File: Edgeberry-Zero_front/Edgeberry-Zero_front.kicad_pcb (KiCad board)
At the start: 2 copper layers, 59.8 x 20.6 mm, 1 part, among them J1 PinSocket_1x04_P2.54mm_Vertic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

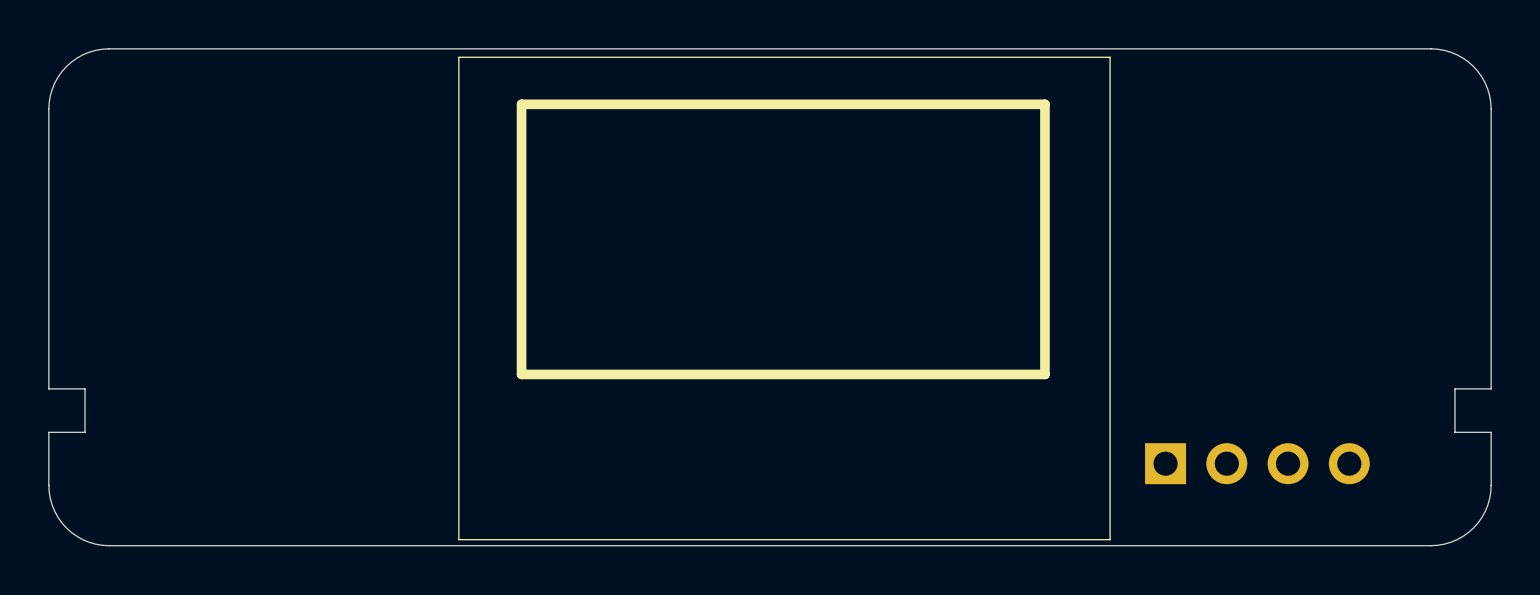
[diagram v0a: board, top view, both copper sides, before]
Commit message: Improvements: C2, J4 (ext)
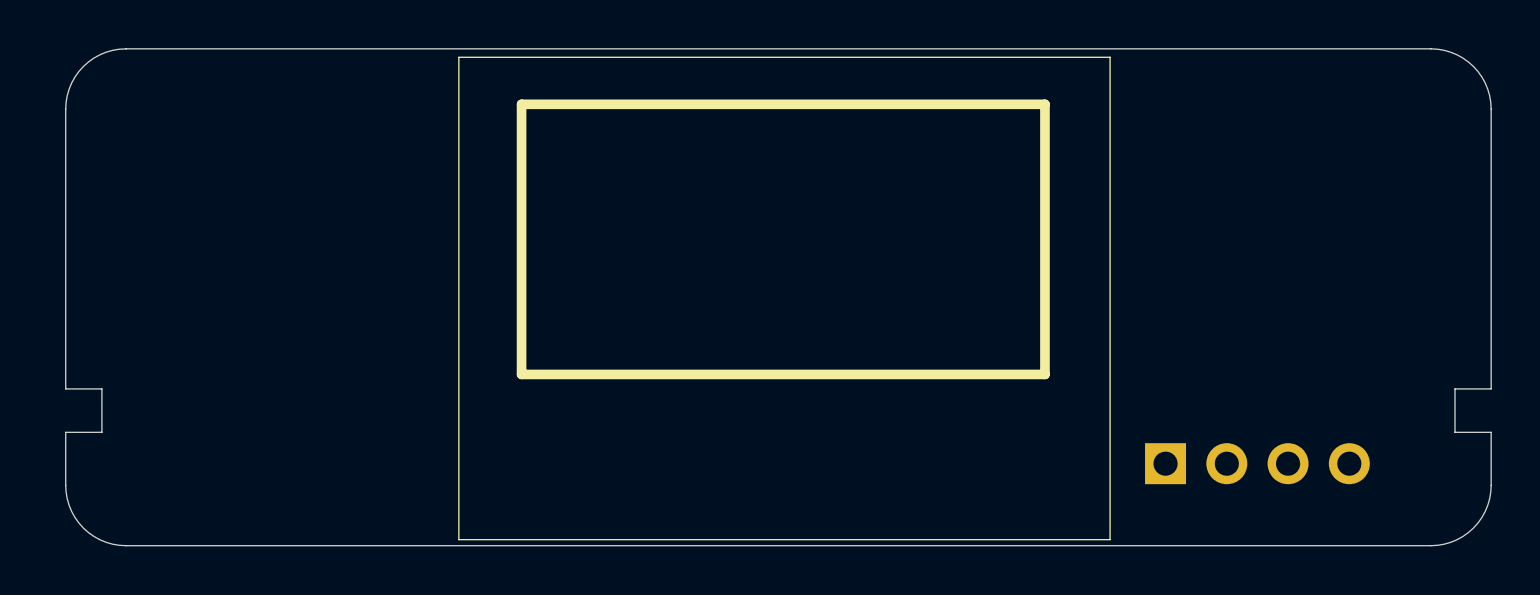
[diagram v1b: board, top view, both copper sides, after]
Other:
- board size 59.8 x 20.6 mm -> 59.1 x 20.6 mm
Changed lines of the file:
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@@
 		)
 		(property "Value" "PinSocket_1x04_P2.54mm_Vertical"
-			(at 7.8 -4.6 180)
+			(at 7.8 -4.6 0)
 			(layer "B.Fab")
 			(hide yes)
@@
 			)
 		)
+		(model "/home/tom/Projects/KiCad_library/3D models/Elecrow_display.step"
+			(offset
+				(xyz -6.9 15.8 -1.6)
+			)
+			(scale
+				(xyz 1 1 1)
+			)
+			(rotate
+				(xyz 0 180 -90)
+			)
+		)
 	)
 	(gr_poly
@@
 	(gr_line
 		(start 188.3 109.7)
-		(end 128.5 109.7)
+		(end 129.2 109.7)
 		(locked yes)
 		(stroke
@@
 	(gr_line
 		(start 186.8 115.3)
-		(end 130 115.3)
+		(end 130.7 115.3)
 		(locked yes)
 		(stroke
@@
 	(gr_line
 		(start 186.8 113.5)
-		(end 130 113.5)
+		(end 130.7 113.5)
 		(locked yes)
 		(stroke
@@
 	)
 	(gr_arc
-		(start 128.5 101.9)
-		(mid 129.232233 100.132233)
-		(end 131 99.4)
+		(start 129.2 101.9)
+		(mid 129.932233 100.132233)
+		(end 131.7 99.4)
 		(locked yes)
 		(stroke
@@
 	(gr_line
 		(start 185.8 99.4)
-		(end 131 99.4)
-		(locked yes)
-		(stroke
-			(width 0.05)
-			(type default)
-		)
-		(layer "Edge.Cuts")
-	)
-	(gr_line
-		(start 130 113.5)
-		(end 128.5 113.5)
-		(locked yes)
-		(stroke
-			(width 0.05)
-			(type default)
-		)
-		(layer "Edge.Cuts")
-	)
-	(gr_line
-		(start 130 113.5)
-		(end 130 115.3)
-		(locked yes)
-		(stroke
-			(width 0.05)
-			(type default)
-		)
-		(layer "Edge.Cuts")
-	)
-	(gr_line
-		(start 131 120)
+		(end 131.7 99.4)
+		(locked yes)
+		(stroke
+			(width 0.05)
+			(type default)
+		)
+		(layer "Edge.Cuts")
+	)
+	(gr_line
+		(start 130.7 113.5)
+		(end 129.2 113.5)
+		(locked yes)
+		(stroke
+			(width 0.05)
+			(type default)
+		)
+		(layer "Edge.Cuts")
+	)
+	(gr_line
+		(start 130.7 113.5)
+		(end 130.7 115.3)
+		(locked yes)
+		(stroke
+			(width 0.05)
+			(type default)
+		)
+		(layer "Edge.Cuts")
+	)
+	(gr_line
+		(start 131.7 120)
 		(end 185.8 120)
 		(locked yes)
@@
 	)
 	(gr_arc
-		(start 131 120)
-		(mid 129.232233 119.267767)
-		(end 128.5 117.5)
+		(start 131.7 120)
+		(mid 129.932233 119.267767)
+		(end 129.2 117.5)
 		(locked yes)
 		(stroke
@@
 	)
 	(gr_line
-		(start 130 115.3)
-		(end 128.5 115.3)
+		(start 130.7 115.3)
+		(end 129.2 115.3)
 		(locked yes)
 		(stroke
@@
 	)
 	(gr_line
-		(start 128.5 113.5)
-		(end 128.5 101.9)
+		(start 129.2 113.5)
+		(end 129.2 101.9)
 		(locked yes)
 		(stroke
@@
 	)
 	(gr_line
-		(start 128.5 117.5)
-		(end 128.5 115.3)
-		(locked yes)
-		(stroke
+		(start 129.2 117.5)
+		(end 129.2 115.3)
+		(locked yes)
+		(stroke

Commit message: cleanup
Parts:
- removed J1: PinSocket_1x04_P2.54mm_Vertical, Connector_PinSocket_2.54mm:PinSocket_1x04_P2.54mm_Vertical
- added REF**: PinHeader_1x04_P2.00mm_Vertical, Connector_PinHeader_2.00mm:PinHeader_1x04_P2.00mm_Vertical, B.Cu at (182.0, 116.3)
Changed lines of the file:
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@@
 	)
 	(net 0 "")
-	(footprint "Connector_PinSocket_2.54mm:PinSocket_1x04_P2.54mm_Vertical"
-		(locked yes)
+	(footprint "Connector_PinHeader_2.00mm:PinHeader_1x04_P2.00mm_Vertical"
 		(layer "B.Cu")
-		(at 174.8 116.6 -90)
-		(descr "Through hole straight socket strip, 1x04, 2.54mm pitch, single row (from Kicad 4.0.7), script generated")
-		(tags "Through hole socket strip THT 1x04 2.54mm single row")
-		(property "Reference" "J1"
-			(at 0 2.77 90)
+		(at 182 116.3 90)
+		(descr "Through hole straight pin header, 1x04, 2.00mm pitch, single row")
+		(tags "Through hole pin header THT 1x04 2.00mm single row")
+		(property "Reference" "REF**"
+			(at 0 2.06 90)
 			(layer "B.SilkS")
 			(effects
@@
 			)
 		)
-		(property "Value" "PinSocket_1x04_P2.54mm_Vertical"
-			(at 7.8 -4.6 0)
+		(property "Value" "PinHeader_1x04_P2.00mm_Vertical"
+			(at 0 -8.06 90)
 			(layer "B.Fab")
-			(hide yes)
 			(effects
 				(font
@@
 			)
 		)
-		(property "Footprint" "Connector_PinSocket_2.54mm:PinSocket_1x04_P2.54mm_Vertical"
-			(at 0 0 90)
+		(property "Footprint" "Connector_PinHeader_2.00mm:PinHeader_1x04_P2.00mm_Vertical"
+			(at 0 0 -90)
 			(unlocked yes)
 			(layer "B.Fab")
@@
 		)
 		(property "Datasheet" ""
-			(at 0 0 90)
+			(at 0 0 -90)
 			(unlocked yes)
 			(layer "B.Fab")
@@
 		)
 		(property "Description" ""
-			(at 0 0 90)
+			(at 0 0 -90)
 			(unlocked yes)
 			(layer "B.Fab")
@@
 		(attr through_hole)
 		(fp_line
-			(start 1.33 1.33)
-			(end 0 1.33)
+			(start 1.06 -7.06)
+			(end -1.06 -7.06)
 			(stroke
 				(width 0.12)
@@
 		)
 		(fp_line
-			(start 1.33 0)
-			(end 1.33 1.33)
+			(start 1.06 -7.06)
+			(end 1.06 -1)
 			(stroke
 				(width 0.12)
@@
 		)
 		(fp_line
-			(start 1.33 -1.27)
-			(end -1.33 -1.27)
+			(start -1.06 -7.06)
+			(end -1.06 -1)
 			(stroke
 				(width 0.12)
@@
 		)
 		(fp_line
-			(start -1.33 -8.95)
-			(end -1.33 -1.27)
+			(start 1.06 -1)
+			(end -1.06 -1)
 			(stroke
 				(width 0.12)
@@
 		)
 		(fp_line
-			(start 1.33 -8.95)
-			(end 1.33 -1.27)
+			(start 0 1.06)
+			(end -1.06 1.06)
 			(stroke
 				(width 0.12)
@@
 		)
 		(fp_line
-			(start 1.33 -8.95)
-			(end -1.33 -8.95)
+			(start -1.06 1.06)
+			(end -1.06 0)
 			(stroke
 				(width 0.12)
@@
 		)
 		(fp_line
-			(start -1.8 1.8)
-			(end -1.8 -9.4)
+			(start 1.5 -7.5)
+			(end -1.5 -7.5)
 			(stroke
 				(width 0.05)
@@
 		)
 		(fp_line
-			(start 1.75 1.8)
-			(end -1.8 1.8)
+			(start -1.5 -7.5)
+			(end -1.5 1.5)
 			(stroke
 				(width 0.05)
@@
 		)
 		(fp_line
-			(start -1.8 -9.4)
-			(end 1.75 -9.4)
+			(start 1.5 1.5)
+			(end 1.5 -7.5)
 			(stroke
 				(width 0.05)
@@
 		)
 		(fp_line
-			(start 1.75 -9.4)
-			(end 1.75 1.8)
+			(start -1.5 1.5)
+			(end 1.5 1.5)
 			(stroke
 				(width 0.05)
@@
 		)
 		(fp_line
-			(start -1.27 1.27)
-			(end -1.27 -8.89)
+			(start 1 -7)
+			(end 1 1)
 			(stroke
 				(width 0.1)
@@
 		)
 		(fp_line
-			(start 0.635 1.27)
-			(end -1.27 1.27)
+			(start -1 -7)
+			(end 1 -7)
 			(stroke
 				(width 0.1)
@@
 		)
 		(fp_line
-			(start 1.27 0.635)
-			(end 0.635 1.27)
+			(start -1 0.5)
+			(end -1 -7)
 			(stroke
 				(width 0.1)
@@
 		)
 		(fp_line
-			(start -1.27 -8.89)
-			(end 1.27 -8.89)
+			(start 1 1)
+			(end -0.5 1)
 			(stroke
 				(width 0.1)
@@
 		)
 		(fp_line
-			(start 1.27 -8.89)
-			(end 1.27 0.635)
+			(start -0.5 1)
+			(end -1 0.5)
 			(stroke
 				(width 0.1)
@@
 		)
 		(fp_text user "${REFERENCE}"
-			(at 0 -3.81 0)
+			(at 0 -3 360)
 			(layer "B.Fab")
 			(effects
@@
 		)
 		(pad "1" thru_hole rect
-			(at 0 0 270)
-			(size 1.7 1.7)
-			(drill 1)
+			(at 0 0 90)
+			(size 1.35 1.35)
+			(drill 0.8)
 			(layers "*.Cu" "*.Mask" "In1.Cu" "In2.Cu" "In3.Cu" "In4.Cu" "In5.Cu" "In6.Cu"
 				"In7.Cu" "In8.Cu" "In9.Cu" "In10.Cu" "In11.Cu" "In12.Cu" "In13.Cu" "In14.Cu"
@@
 		)
 		(pad "2" thru_hole oval
-			(at 0 -2.54 270)
-			(size 1.7 1.7)
-			(drill 1)
+			(at 0 -2 90)
+			(size 1.35 1.35)
+			(drill 0.8)
 			(layers "*.Cu" "*.Mask" "In1.Cu" "In2.Cu" "In3.Cu" "In4.Cu" "In5.Cu" "In6.Cu"
 				"In7.Cu" "In8.Cu" "In9.Cu" "In10.Cu" "In11.Cu" "In12.Cu" "In13.Cu" "In14.Cu"
@@
 		)
 		(pad "3" thru_hole oval
-			(at 0 -5.08 270)
-			(size 1.7 1.7)
-			(drill 1)
+			(at 0 -4 90)
+			(size 1.35 1.35)
+			(drill 0.8)
 			(layers "*.Cu" "*.Mask" "In1.Cu" "In2.Cu" "In3.Cu" "In4.Cu" "In5.Cu" "In6.Cu"
 				"In7.Cu" "In8.Cu" "In9.Cu" "In10.Cu" "In11.Cu" "In12.Cu" "In13.Cu" "In14.Cu"
@@
 		)
 		(pad "4" thru_hole oval
-			(at 0 -7.62 270)
-			(size 1.7 1.7)
-			(drill 1)
+			(at 0 -6 90)
+			(size 1.35 1.35)
+			(drill 0.8)
 			(layers "*.Cu" "*.Mask" "In1.Cu" "In2.Cu" "In3.Cu" "In4.Cu" "In5.Cu" "In6.Cu"
 				"In7.Cu" "In8.Cu" "In9.Cu" "In10.Cu" "In11.Cu" "In12.Cu" "In13.Cu" "In14.Cu"
@@
 			(remove_unused_layers no)
 		)
-		(model "${KICAD8_3DMODEL_DIR}/Connector_PinSocket_2.54mm.3dshapes/PinSocket_1x04_P2.54mm_Vertical.wrl"
-			(hide yes)
+		(model "${KICAD8_3DMODEL_DIR}/Connector_PinHeader_2.00mm.3dshapes/PinHeader_1x04_P2.00mm_Vertical.wrl"
 			(offset
 				(xyz 0 0 0)
@@
 			(rotate
 				(xyz 0 0 0)
-			)
-		)
-		(model "/home/tom/Projects/KiCad_library/3D models/Elecrow_display.step"
-			(offset
-				(xyz -6.9 15.8 -1.6)
-			)
-			(scale
-				(xyz 1 1 1)
-			)
-			(rotate
-				(xyz 0 180 -90)
 			)
 		)
@@
 		(layer "Dwgs.User")
 		(pts
-			(xy 186.8 115.3) (xy 175 115.2)
+			(xy 186.8 115.3) (xy 176 116.3)
 		)
 		(height 7.1)
 		(orientation 0)
-		(gr_text "11.8000 mm"
-			(at 180.9 121.25 0)
+		(gr_text "10.8000 mm"
+			(at 181.4 121.25 0)
 			(layer "Dwgs.User")
 			(effects
@@
 			(layer "Dwgs.User")
 			(effects
+				(font
+					(size 1 1)
+					(thickness 0.15)
+				)
+			)
+		)
+		(format
+			(prefix "")
+			(suffix "")
+			(units 3)
+			(units_format 1)
+			(precision 4)
+		)
+		(style
+			(thickness 0.1)
+			(arrow_length 1.27)
+			(text_position_mode 0)
+			(extension_height 0.58642)
+			(extension_offset 0.5) keep_text_aligned)
+	)
+	(dimension
+		(type orthogonal)
+		(layer "Dwgs.User")
+		(pts
+			(xy 129.2 101.9) (xy 188.3 101.9)
+		)
+		(height -6.5)
+		(orientation 0)
+		(gr_text "59.1000 mm"
+			(at 158.75 94.25 0)
+			(layer "Dwgs.User")
+			(effects
+				(font
+					(size 1 1)
+					(thickness 0.15)
+				)
+			)
+		)
+		(format
+			(prefix "")
+			(suffix "")
+			(units 3)
+			(units_format 1)
+			(precision 4)
+		)
+		(style
+			(thickness 0.1)
+			(arrow_length 1.27)
+			(text_position_mode 0)
+			(extension_height 0.58642)
+			(extension_offset 0.5) keep_text_aligned)
+	)
+	(dimension
+		(type orthogonal)
+		(layer "Dwgs.User")
+		(pts
+			(xy 130.7 113.5) (xy 186.8 113.5)
+		)
+		(height -15.5)
+		(orientation 0)
+		(gr_text "56.1000 mm"
+			(at 158.75 96.85 0)
+			(layer "Dwgs.User")
+			(effects
